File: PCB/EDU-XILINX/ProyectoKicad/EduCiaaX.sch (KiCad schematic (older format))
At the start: 0 parts

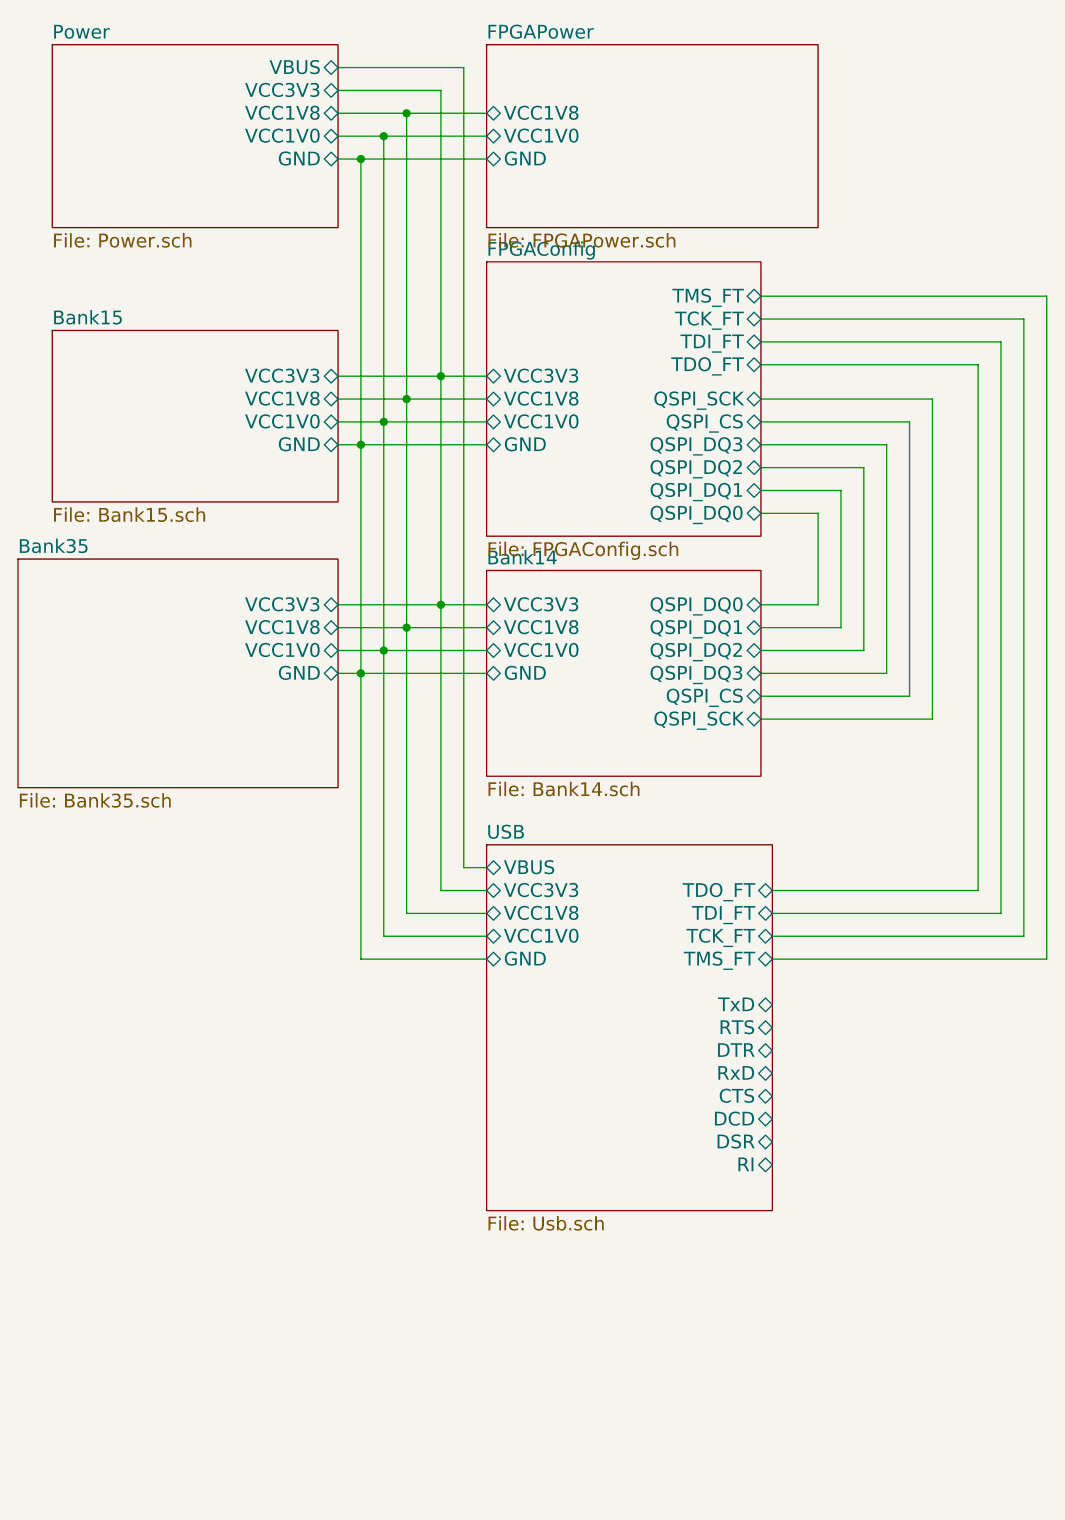
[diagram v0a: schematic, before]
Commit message: Conexion Puerto Serie-FPGA
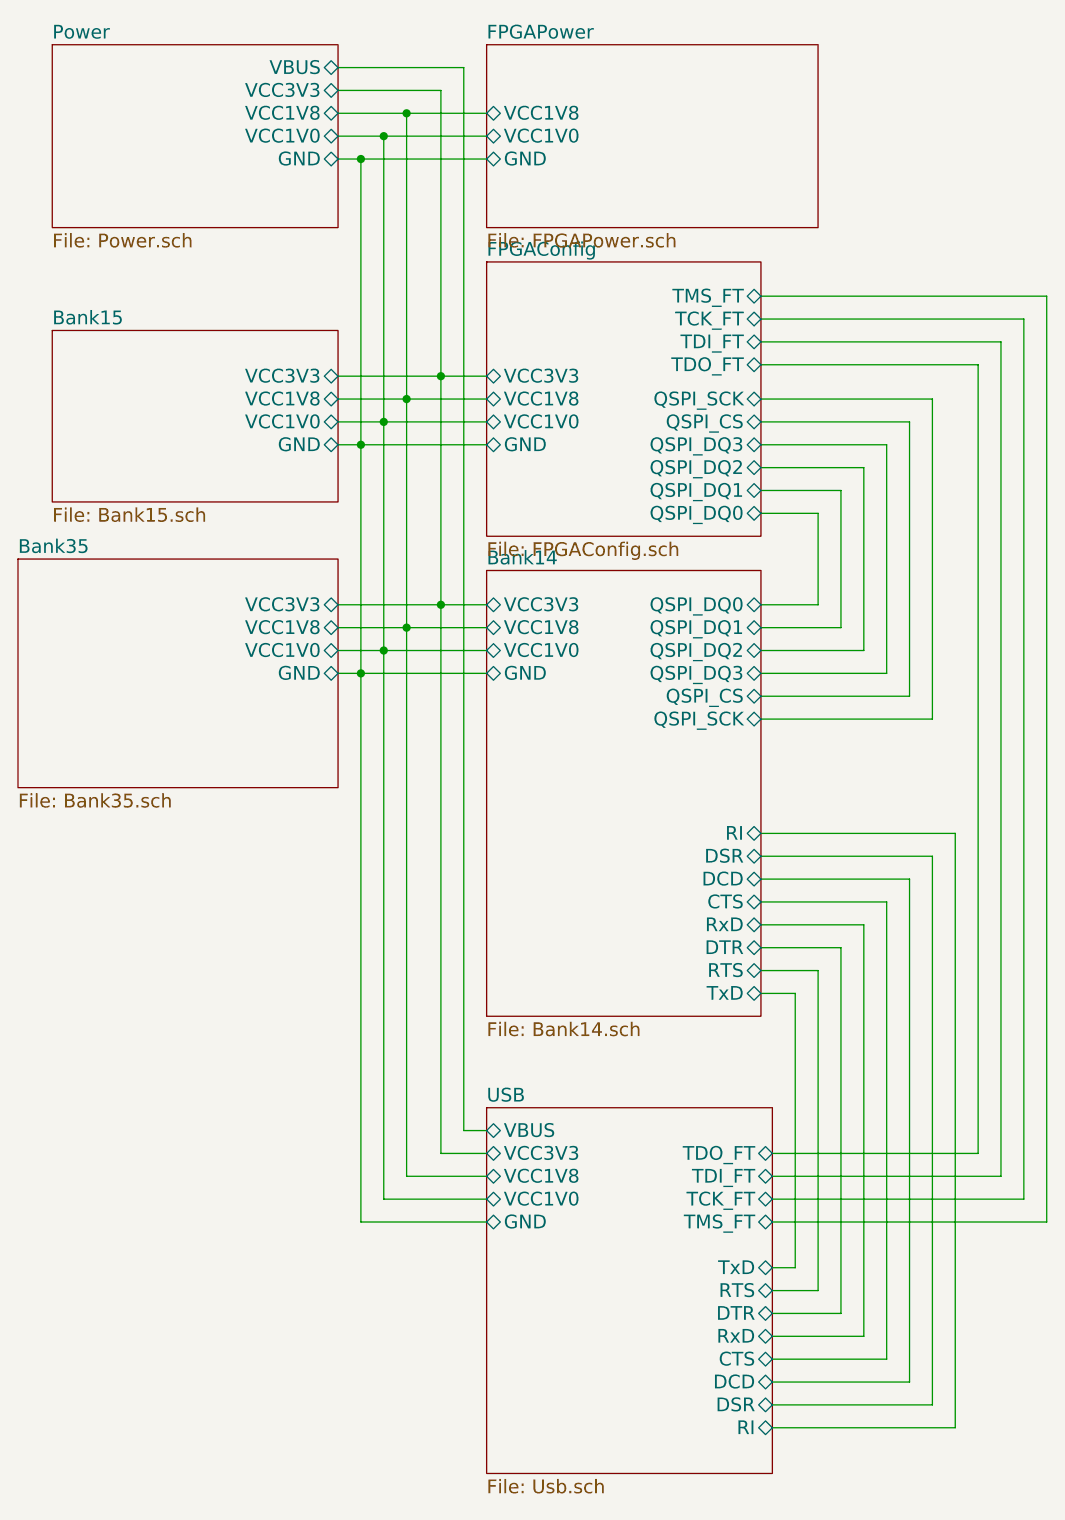
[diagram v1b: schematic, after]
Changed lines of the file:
@@
 	2300 2500 2950 2500
 Wire Wire Line
-	2750 1250 2750 4750
+	2750 1250 2750 5900
 Wire Wire Line
 	2750 1250 2300 1250
@@
 	2300 2600 2950 2600
 Wire Wire Line
-	2600 1350 2600 4850
+	2600 1350 2600 6000
 Connection ~ 2600 1350
 Wire Wire Line
 	2300 2700 2950 2700
 Wire Wire Line
-	2500 1450 2500 4950
+	2500 1450 2500 6100
 Connection ~ 2500 1450
 Wire Wire Line
 	2300 2800 2950 2800
 Wire Wire Line
-	2400 1550 2400 5050
+	2400 1550 2400 6200
 Connection ~ 2400 1550
 $Sheet
-S 2950 3350 1200 900
+S 2950 3350 1200 1950
 U 5611B803
 F0 "Bank14" 60
@@
 F10 "QSPI_SCK" B R 4150 4000 60
 F11 "GND" B L 2950 3800 60
+F12 "TxD" B R 4150 5200 60
+F13 "RTS" B R 4150 5100 60
+F14 "DTR" B R 4150 5000 60
+F15 "RxD" B R 4150 4900 60
+F16 "CTS" B R 4150 4800 60
+F17 "DCD" B R 4150 4700 60
+F18 "DSR" B R 4150 4600 60
+F19 "RI" B R 4150 4500 60
 $EndSheet
 Wire Wire Line
@@
 F5 "GND" B R 2300 3800 60
 $EndSheet
-Wire Wire Line
-	2750 4750 2950 4750
 Connection ~ 2750 3500
-Wire Wire Line
-	2600 4850 2950 4850
 Connection ~ 2600 3600
-Wire Wire Line
-	2500 4950 2950 4950
 Connection ~ 2500 3700
-Wire Wire Line
-	2400 5050 2950 5050
 Connection ~ 2400 3800
 $Sheet
@@
 $EndSheet
 $Sheet
-S 2950 4550 1250 1600
+S 2950 5700 1250 1600
 U 561EC105
 F0 "USB" 60
 F1 "Usb.sch" 60
-F2 "VCC3V3" B L 2950 4750 60
-F3 "VCC1V8" B L 2950 4850 60
-F4 "VCC1V0" B L 2950 4950 60
-F5 "GND" B L 2950 5050 60
-F6 "TMS_FT" B R 4200 5050 60
-F7 "TCK_FT" B R 4200 4950 60
-F8 "TDI_FT" B R 4200 4850 60
-F9 "TDO_FT" B R 4200 4750 60
-F10 "VBUS" B L 2950 4650 60
-F11 "TxD" B R 4200 5250 60
-F12 "RTS" B R 4200 5350 60
-F13 "DTR" B R 4200 5450 60
-F14 "RxD" B R 4200 5550 60
-F15 "CTS" B R 4200 5650 60
-F16 "DCD" B R 4200 5750 60
-F17 "DSR" B R 4200 5850 60
-F18 "RI" B R 4200 5950 60
+F2 "VCC3V3" B L 2950 5900 60
+F3 "VCC1V8" B L 2950 6000 60
+F4 "VCC1V0" B L 2950 6100 60
+F5 "GND" B L 2950 6200 60
+F6 "TMS_FT" B R 4200 6200 60
+F7 "TCK_FT" B R 4200 6100 60
+F8 "TDI_FT" B R 4200 6000 60
+F9 "TDO_FT" B R 4200 5900 60
+F10 "VBUS" B L 2950 5800 60
+F11 "TxD" B R 4200 6400 60
+F12 "RTS" B R 4200 6500 60
+F13 "DTR" B R 4200 6600 60
+F14 "RxD" B R 4200 6700 60
+F15 "CTS" B R 4200 6800 60
+F16 "DCD" B R 4200 6900 60
+F17 "DSR" B R 4200 7000 60
+F18 "RI" B R 4200 7100 60
 $EndSheet
 Wire Wire Line
@@
 	4900 2600 4900 4000
 Wire Wire Line
-	4200 4750 5100 4750
-Wire Wire Line
-	5100 4750 5100 2450
+	5100 2450 5100 5900
 Wire Wire Line
 	5100 2450 4150 2450
@@
 	4150 2350 5200 2350
 Wire Wire Line
-	5200 2350 5200 4850
-Wire Wire Line
-	5200 4850 4200 4850
-Wire Wire Line
-	4200 4950 5300 4950
-Wire Wire Line
-	5300 4950 5300 2250
+	5200 2350 5200 6000
+Wire Wire Line
+	5300 2250 5300 6100
 Wire Wire Line
 	5300 2250 4150 2250
@@
 	4150 2150 5400 2150
 Wire Wire Line
-	5400 2150 5400 5050
-Wire Wire Line
-	5400 5050 4200 5050
-Wire Wire Line
-	2950 4650 2850 4650
-Wire Wire Line
-	2850 4650 2850 1150
+	5400 2150 5400 6200
+Wire Wire Line
+	2850 1150 2850 5800
 Wire Wire Line
 	2850 1150 2300 1150
+Wire Wire Line
+	2850 5800 2950 5800
+Wire Wire Line
+	2750 5900 2950 5900
+Wire Wire Line
+	2600 6000 2950 6000
+Wire Wire Line
+	2500 6100 2950 6100
+Wire Wire Line
+	2400 6200 2950 6200
+Wire Wire Line
+	5100 5900 4200 5900
+Wire Wire Line
+	5200 6000 4200 6000
+Wire Wire Line
+	5300 6100 4200 6100
+Wire Wire Line
+	5400 6200 4200 6200
+Wire Wire Line
+	4200 6400 4300 6400
+Wire Wire Line
+	4300 6400 4300 5200
+Wire Wire Line
+	4300 5200 4150 5200
+Wire Wire Line
+	4150 5100 4400 5100
+Wire Wire Line
+	4400 5100 4400 6500
+Wire Wire Line
+	4400 6500 4200 6500
+Wire Wire Line
+	4200 6600 4500 6600
+Wire Wire Line
+	4500 6600 4500 5000
+Wire Wire Line
+	4500 5000 4150 5000
+Wire Wire Line
+	4150 4900 4600 4900
+Wire Wire Line
+	4600 4900 4600 6700
+Wire Wire Line
+	4600 6700 4200 6700
+Wire Wire Line
+	4200 6800 4700 6800
+Wire Wire Line
+	4700 6800 4700 4800
+Wire Wire Line
+	4700 4800 4150 4800
+Wire Wire Line
+	4150 4700 4800 4700
+Wire Wire Line
+	4800 4700 4800 6900
+Wire Wire Line
+	4800 6900 4200 6900
+Wire Wire Line
+	4200 7000 4900 7000
+Wire Wire Line
+	4900 7000 4900 4600
+Wire Wire Line
+	4900 4600 4150 4600
+Wire Wire Line
+	4150 4500 5000 4500
+Wire Wire Line
+	5000 4500 5000 7100
+Wire Wire Line
+	5000 7100 4200 7100
 $EndSCHEMATC
